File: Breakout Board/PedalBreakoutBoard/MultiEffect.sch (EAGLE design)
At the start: 65 parts, among them IC1 LD1117V, IC2 MCP6004P, U1 OPA1652AID

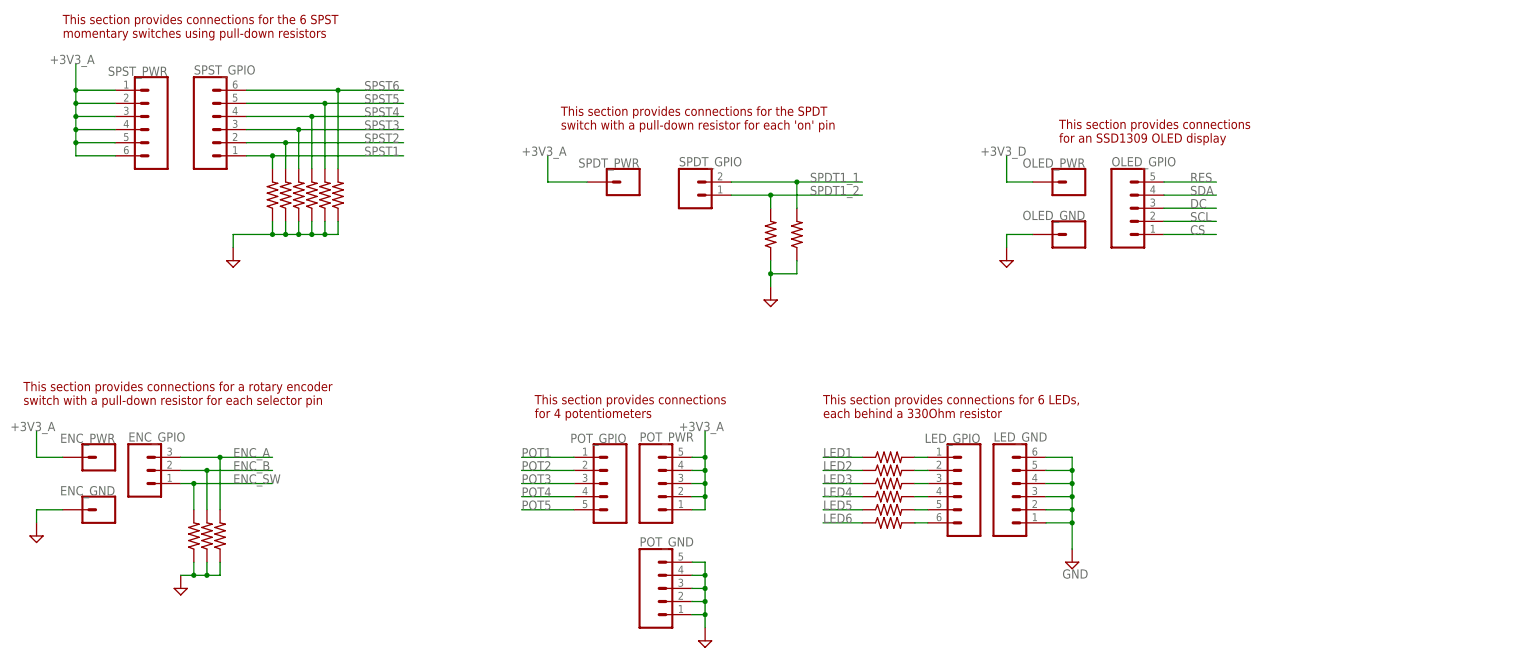
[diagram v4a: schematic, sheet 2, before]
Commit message: DP-6 - Add additional access to GPIO pins
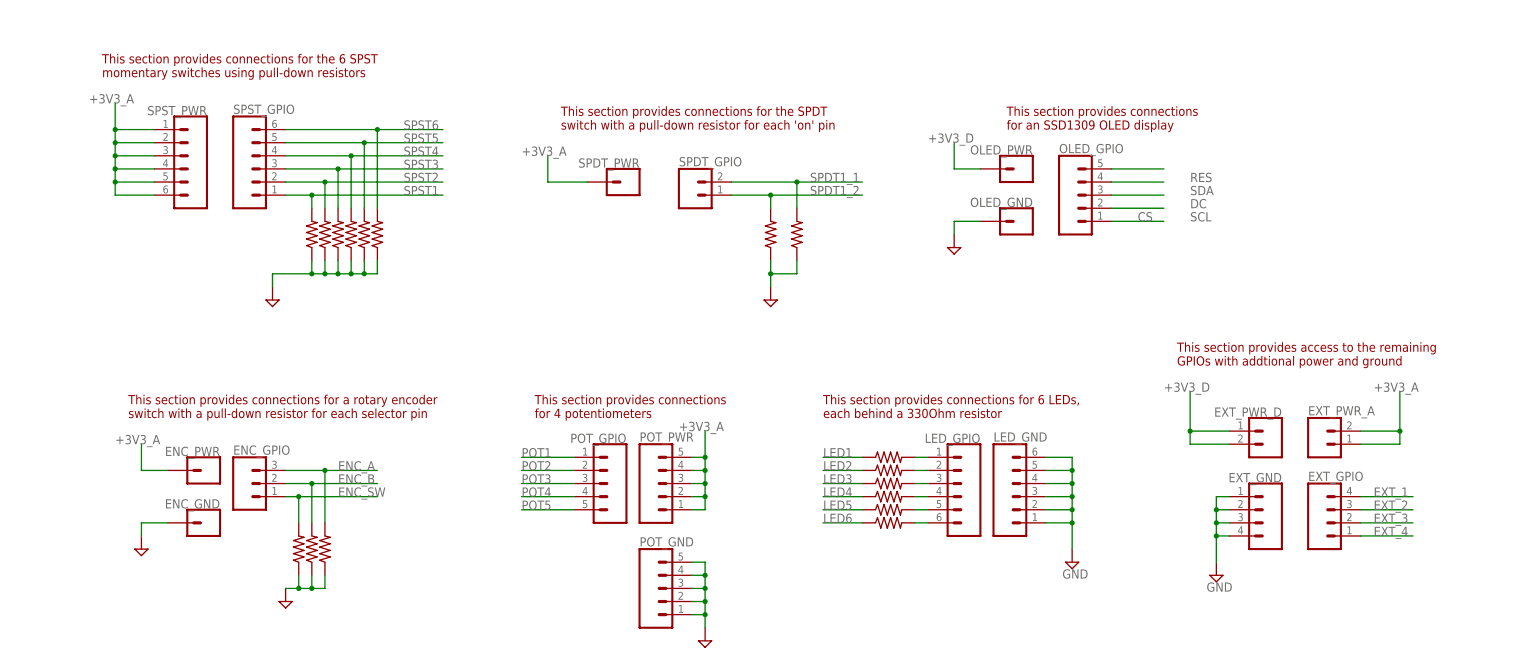
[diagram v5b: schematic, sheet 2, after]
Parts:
- added EXT_GND, EXT_GPIO: (no value), SparkFun-Connectors:CONN_04
- added EXT_PWR_A, EXT_PWR_D: (no value), SparkFun-Connectors:CONN_02
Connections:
- removed net HEX_1: SEED.GPIO30(USB_HS_D_-)
- new net EXT_1: EXT_GPIO.4, SEED.GPIO7(SDMMC1_CK)
- new net EXT_2: EXT_GPIO.3, SEED.GPIO15(USART1_RX)
- new net EXT_3: EXT_GPIO.2, SEED.GPIO30(USB_HS_D_-)
- new net EXT_4: EXT_GPIO.1, SEED.GPIO31(USB_HS_D+)
- net +3V3_A: now also EXT_PWR_A.1, EXT_PWR_A.2
- net +3V3_D: now also EXT_PWR_D.1, EXT_PWR_D.2
- net GND: now also EXT_GND.1, EXT_GND.2, EXT_GND.3, EXT_GND.4
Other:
- note added: "This section provides access to the remaining GPIOs with addtional power and ground"
- moved on the sheet: ENC_GND, ENC_GPIO, ENC_PWR, OLED_GND, OLED_GPIO, OLED_PWR, SPST_GPIO, SPST_PWR

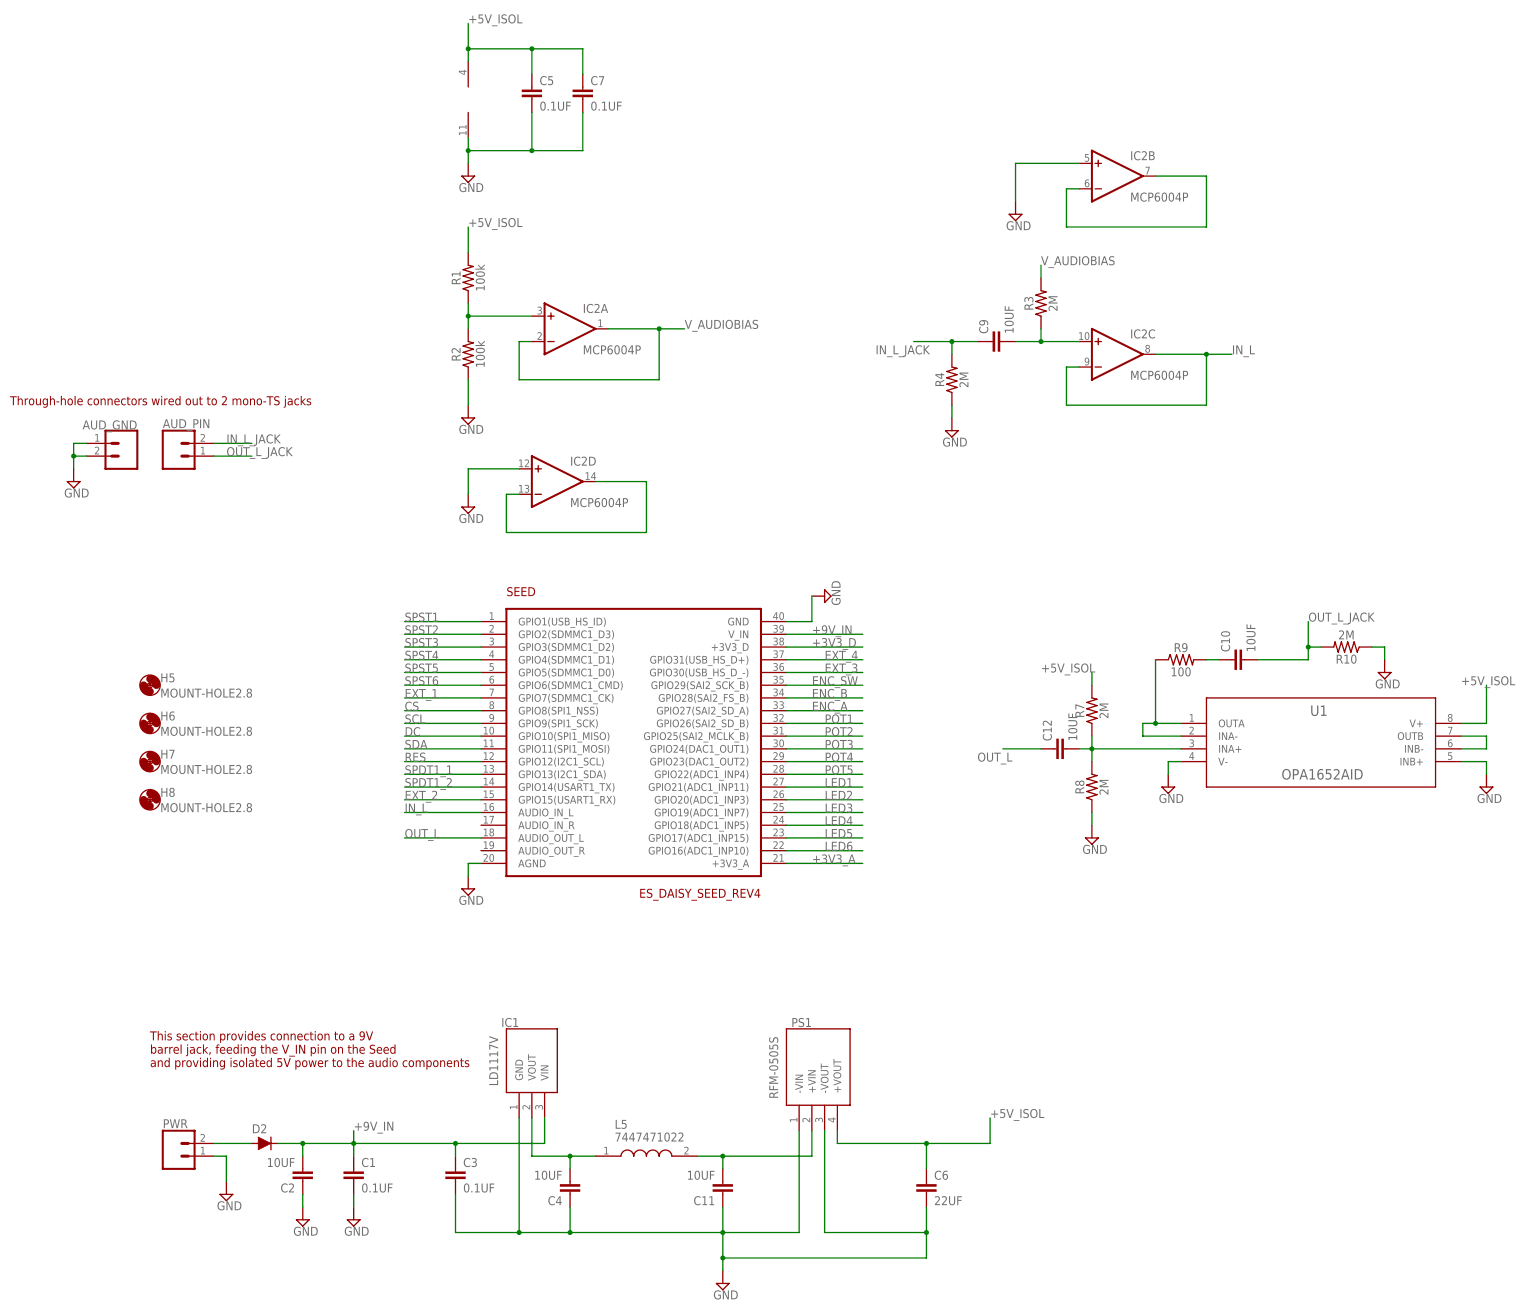
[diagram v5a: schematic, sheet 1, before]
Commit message: DP-97 - Update multi-effect with new grounding scheme
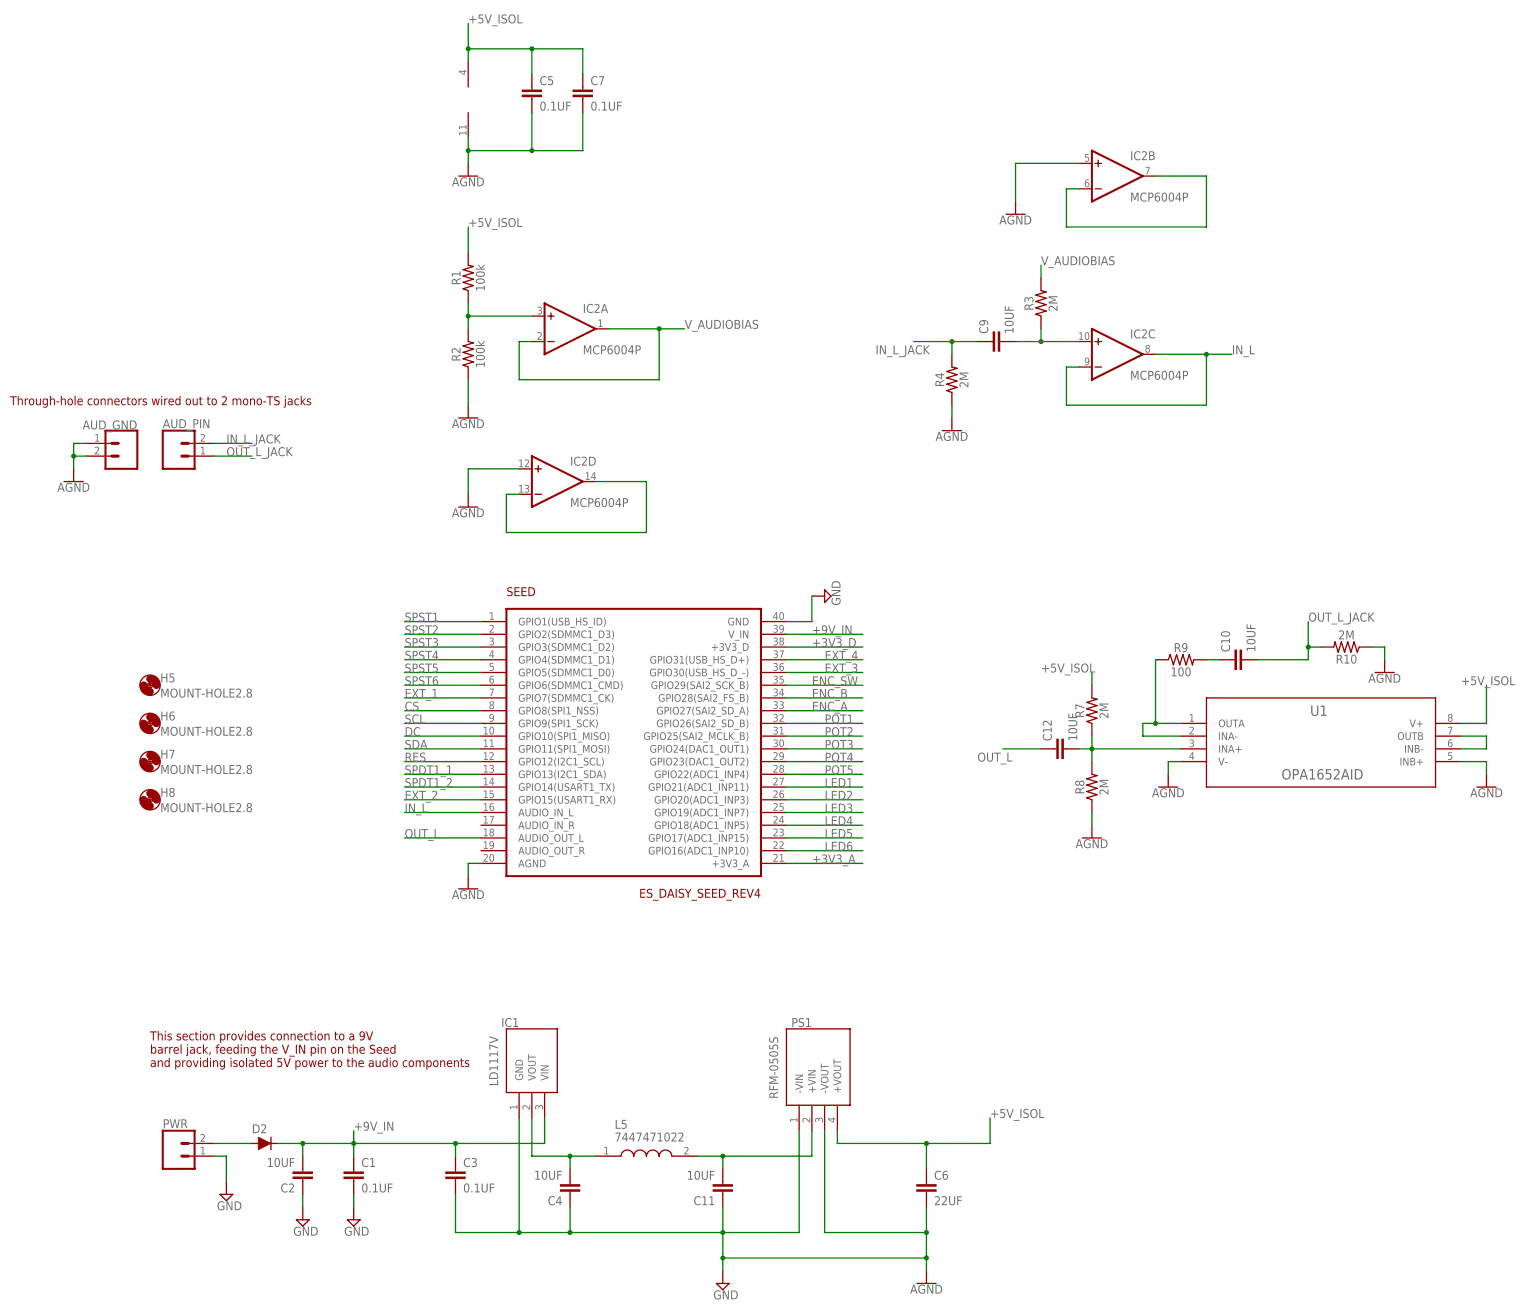
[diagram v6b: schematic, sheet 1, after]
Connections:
- new net AGND: AUD_GND.1, AUD_GND.2, C5.2, C7.2, IC2B.+IN, IC2D.+IN, IC2P.V-, R10.1, R2.1, R4.1, R8.1, SEED.AGND, U1.INB+, U1.V-
- net GND: no longer AUD_GND.1, AUD_GND.2, C5.2, C7.2, IC2B.+IN, IC2D.+IN, IC2P.V-, R10.1, R2.1, R4.1, R8.1, SEED.AGND, U1.INB+, U1.V-
